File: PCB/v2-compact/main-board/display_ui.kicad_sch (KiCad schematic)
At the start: 0 parts

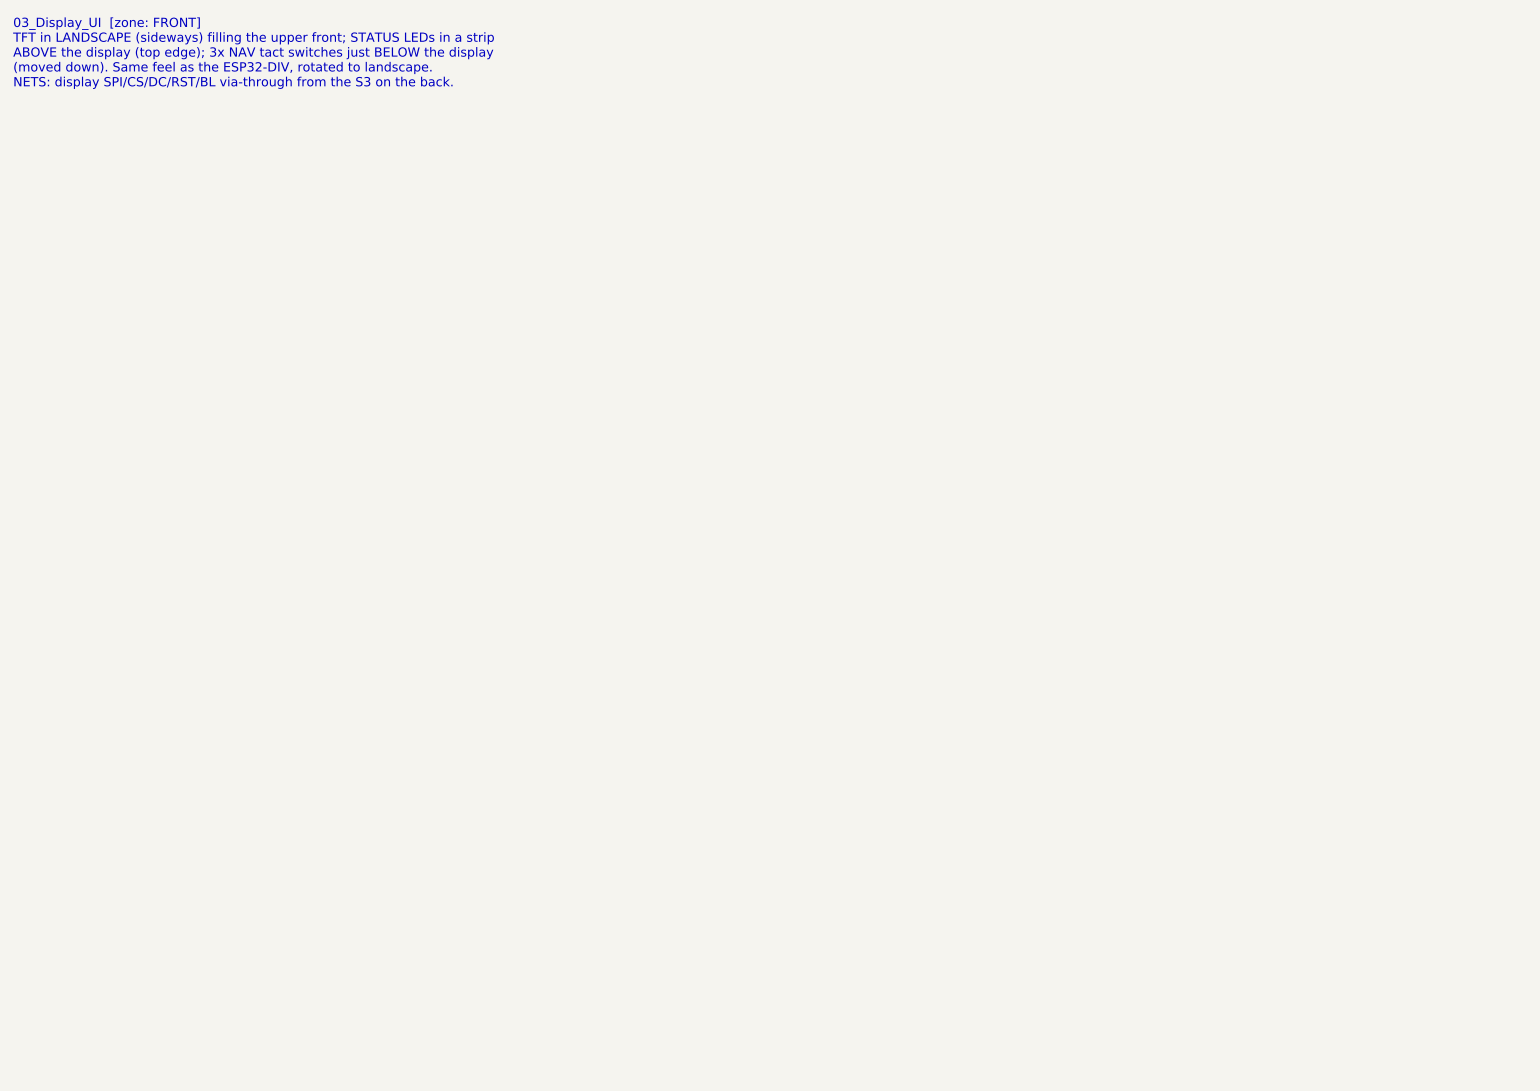
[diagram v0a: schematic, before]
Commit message: Schematics: main board ESP32-S3, microSD, and display/UI sheets
- 02_ESP32-S3: the brain. Shared SPI (LCD_SCK/MOSI + SD_MISO) for TFT and
  microSD, USB data to the USB-C through the ESD, and the full J1 interface to
  the shield (C5 UART + DRDY, I2C to PN532, RV1106 UART, IR, 1-Wire). EN/boot RC
  + decoupling.
- 04_microSD: SPI-mode card with CS pull-up + decoupling.
- 03_Display_UI: SPI TFT header, five nav buttons to GND, two status LEDs.

Netlist-verified: the S3 ties in the other end of every J1 net (isolated labels
on the main board dropped from 12 to 1).
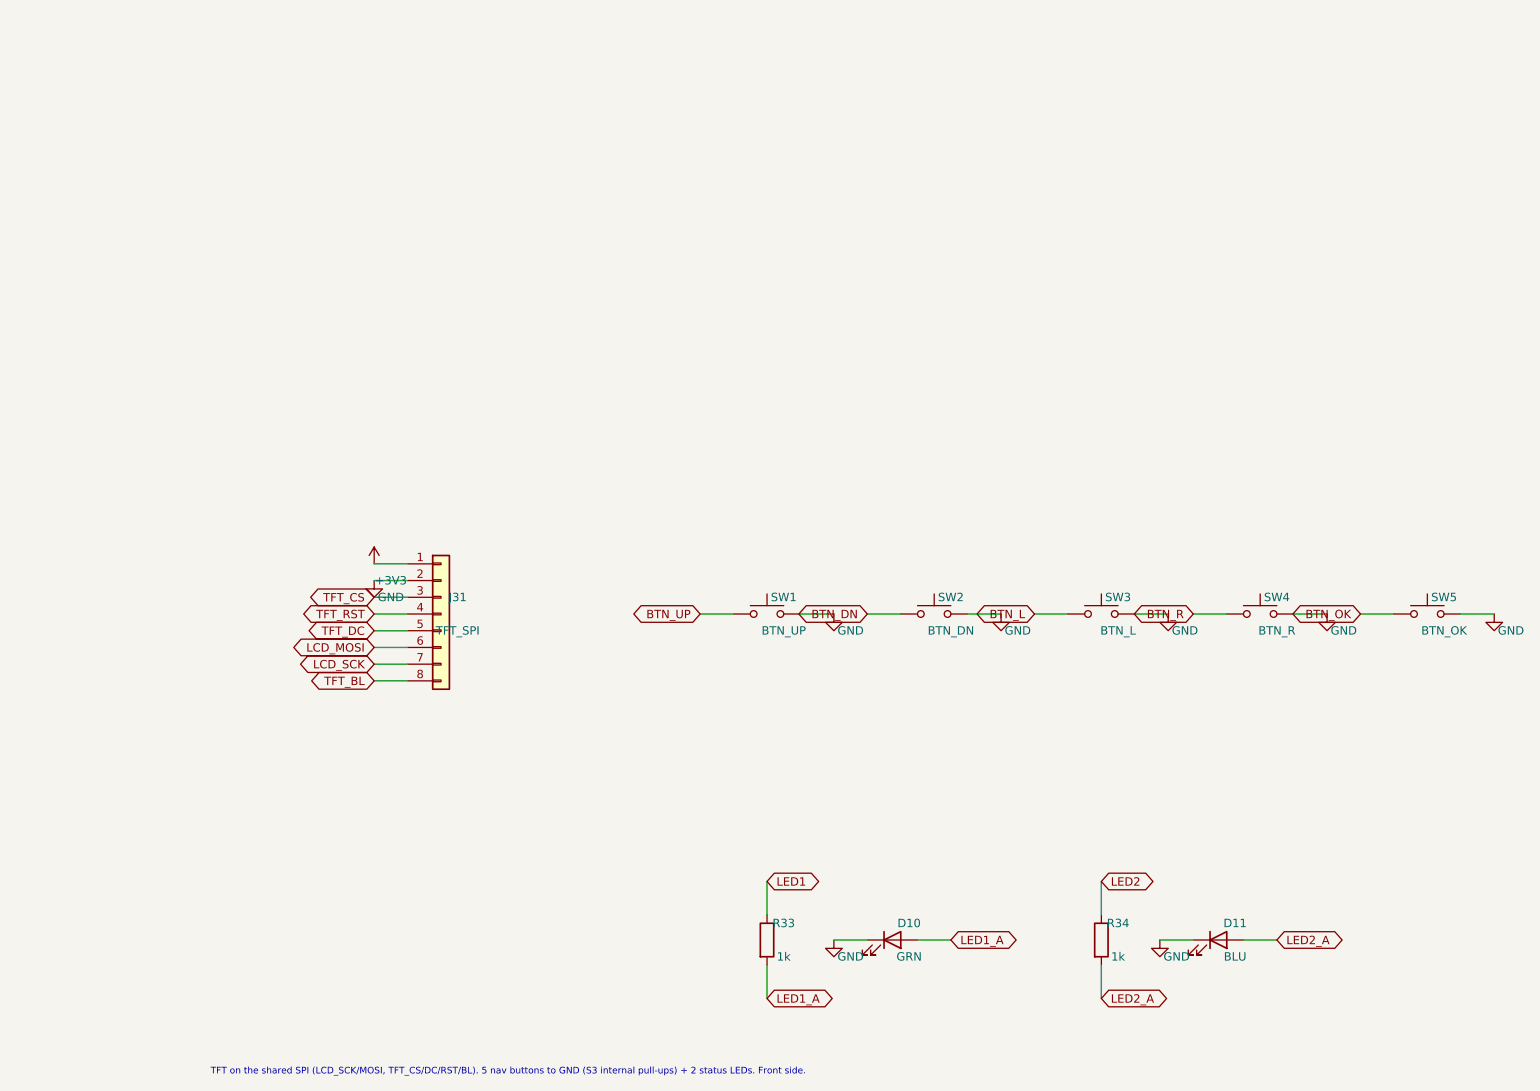
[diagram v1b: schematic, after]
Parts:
- added D10: GRN, LED_SMD:LED_0805_2012Metric, symbol Device:LED
- added D11: BLU, LED_SMD:LED_0805_2012Metric, symbol Device:LED
- added J31: TFT_SPI, Connector_PinHeader_2.54mm:PinHeader_1x08_P2.54mm_Vertical, symbol Connector_Generic:Conn_01x08
- added R33, R34: 1k, Resistor_SMD:R_0402_1005Metric, symbol Device:R
- added SW1: BTN_UP, Button_Switch_THT:SW_PUSH_6mm, symbol Switch:SW_Push
- added SW2: BTN_DN, Button_Switch_THT:SW_PUSH_6mm, symbol Switch:SW_Push
- added SW3: BTN_L, Button_Switch_THT:SW_PUSH_6mm, symbol Switch:SW_Push
- added SW4: BTN_R, Button_Switch_THT:SW_PUSH_6mm, symbol Switch:SW_Push
- added SW5: BTN_OK, Button_Switch_THT:SW_PUSH_6mm, symbol Switch:SW_Push
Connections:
- new net +3V3: J31.1 (Pin_1)
- new net BTN_DN: SW2.1
- new net BTN_L: SW3.1
- new net BTN_OK: SW5.1
- new net BTN_R: SW4.1
- new net BTN_UP: SW1.1
- new net GND: D10.1 (K), D11.1 (K), J31.2 (Pin_2), SW1.2, SW2.2, SW3.2, SW4.2, SW5.2
- new net LCD_MOSI: J31.6 (Pin_6)
- new net LCD_SCK: J31.7 (Pin_7)
- new net LED1: R33.1
- new net LED1_A: D10.2 (A), R33.2
- new net LED2: R34.1
- new net LED2_A: D11.2 (A), R34.2
- new net TFT_BL: J31.8 (Pin_8)
- new net TFT_CS: J31.3 (Pin_3)
- new net TFT_DC: J31.5 (Pin_5)
- new net TFT_RST: J31.4 (Pin_4)
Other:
- note added: "TFT on the shared SPI (LCD_SCK/MOSI, TFT_CS/DC/RST/BL). 5 nav buttons to GND (S3 internal pull-ups) + 2 status LEDs. Front side."
- note removed: "03_Display_UI [zone: FRONT] TFT in LANDSCAPE (sideways) filling the upper front; STATUS LEDs in a strip ABOVE the display (top edge); 3x NAV tact switches just BELOW the display (moved down). Same feel as the ESP32-DIV, rotated to landscape. NETS: display SPI/CS/DC/RST/BL via-through from the S3 on the back."
